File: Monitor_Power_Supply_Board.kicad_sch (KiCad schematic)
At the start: 12 parts, among them J1 Conn_01x02, J2 Conn_01x02, J3 Conn_01x02

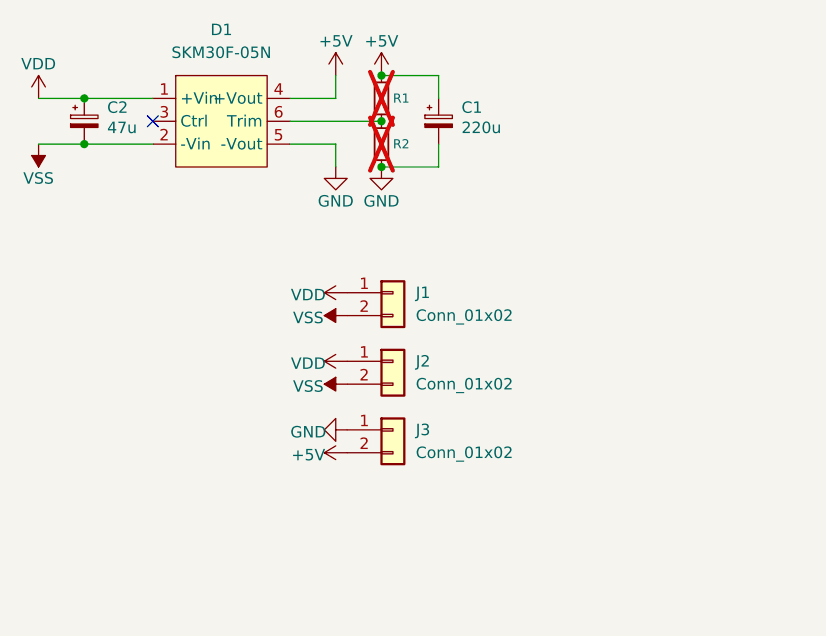
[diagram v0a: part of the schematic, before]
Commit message: VER1.0: добавил разъем для вентилятора и индикацию питания
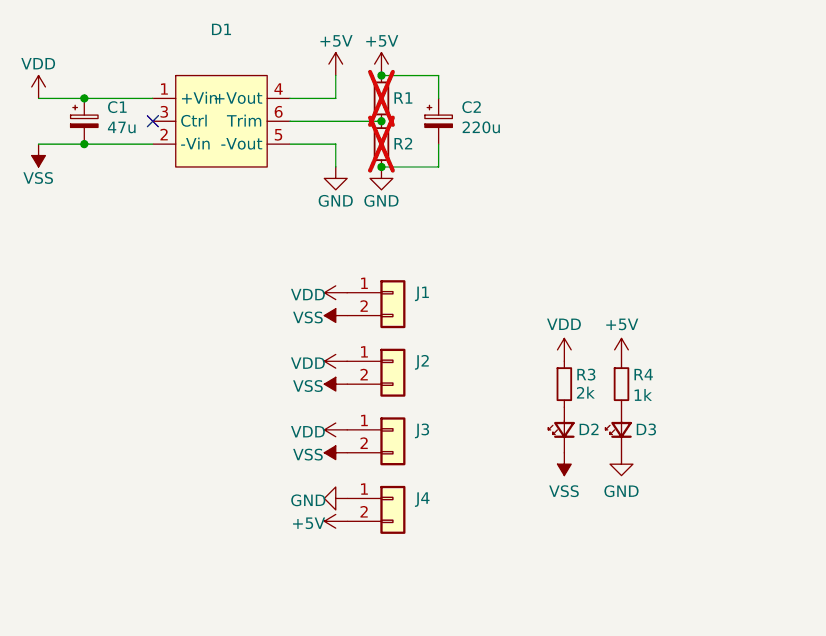
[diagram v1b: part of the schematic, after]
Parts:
- added D2, D3: ~, LED_SMD:LED_0805_2012Metric_Pad1.15x1.40mm_HandSolder, symbol Device:LED_Small
- added J3: ~, Connector_Molex:Molex_Mini-Fit_Jr_5569-02A2_2x01_P4.20mm_Horizontal, symbol Connector_Generic:Conn_01x02
- added R3: 2k, Resistor_SMD:R_0805_2012Metric_Pad1.20x1.40mm_HandSolder, symbol Device:R_Small
- added R4: 1k, Resistor_SMD:R_0805_2012Metric_Pad1.20x1.40mm_HandSolder, symbol Device:R_Small
- C1: renamed from C2; Product Name (none) -> CA45-D025K476T
- C2: renamed from C1; Product Name (none) -> CA45-C010K227T
- D1: value SKM30F-05N -> ~; Product Name (none) -> SKM30F-05N
- J1, J2: value Conn_01x02 -> ~; Product Name (none) -> DS1073-01-2X1MR3T6
- J4: renamed from J3; value Conn_01x02 -> ~; Product Name (none) -> DS1073-01-2X1MR3T6
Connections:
- net +5V: now also R4.1
- net GND: now also D3.1 (K)
- net VDD: now also J3.1 (Pin_1), R3.1
- net VSS: now also D2.1 (K), J3.2 (Pin_2)
- new net: D3.2 (A), R4.2
- new net: D2.2 (A), R3.2
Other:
- moved on the sheet: J4

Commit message: VER1.0: отправил в резонит
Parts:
- C1, C2: Description P/N (none) -> Tantalum Capacitor
- D1: Description P/N (none) -> DCDC
- D2, D3: Description P/N (none) -> Green LED
- J1, J2, J3, J4: Description P/N (none) -> Connector
- R1, R2, R3, R4: Description P/N (none) -> Resistor SMD
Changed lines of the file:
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@@
 			)
 		)
-		(property "Description P/N" ""
+		(property "Description P/N" "Green LED"
 			(at 189.23 130.81 90)
 			(effects
@@
 			)
 		)
-		(property "Description P/N" ""
+		(property "Description P/N" "Connector"
 			(at 163.83 138.43 0)
 			(effects
@@
 			)
 		)
-		(property "Description P/N" ""
+		(property "Description P/N" "Tantalum Capacitor"
 			(at 168.91 96.52 0)
 			(effects
@@
 			)
 		)
-		(property "Description P/N" ""
+		(property "Description P/N" "Connector"
 			(at 163.83 115.57 0)
 			(effects
@@
 			)
 		)
-		(property "Description P/N" ""
+		(property "Description P/N" "Resistor SMD"
 			(at 189.23 125.73 0)
 			(effects
@@
 			)
 		)
-		(property "Description P/N" ""
+		(property "Description P/N" "Tantalum Capacitor"
 			(at 129.54 96.52 0)
 			(effects
@@
 			)
 		)
-		(property "Description P/N" ""
+		(property "Description P/N" "Green LED"
 			(at 182.88 130.81 90)
 			(effects
@@
 			)
 		)
-		(property "Description P/N" ""
+		(property "Description P/N" "Resistor SMD"
 			(at 162.56 99.06 0)
 			(effects
@@
 			)
 		)
-		(property "Description P/N" ""
+		(property "Description P/N" "Resistor SMD"
 			(at 182.88 125.73 0)
 			(effects
@@
 			)
 		)
-		(property "Description P/N" ""
+		(property "Description P/N" "Resistor SMD"
 			(at 162.56 93.98 0)
 			(effects
@@
 			)
 		)
-		(property "Description P/N" ""
+		(property "Description P/N" "Connector"
 			(at 163.83 123.19 0)
 			(effects
@@
 			)
 		)
-		(property "Description P/N" ""
+		(property "Description P/N" "DCDC"
 			(at 144.78 91.44 0)
 			(effects
@@
 			)
 		)
-		(property "Description P/N" ""
+		(property "Description P/N" "Connector"
 			(at 163.83 130.81 0)
 			(effects

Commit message: VER1.0: добавил кд в папку Docs
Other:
- note added: "1 Перечень элементов см. НВЦТ.0001.0600.200 ПЭ3."
- note added: "Индикация питания"
- note added: "Механические отверстия"
- note added: "НВЦТ.0001.0600.200"
- note added: "ООО "Электротранспорнтые"
- note added: "Питание +5В."
- note added: "Разъёмы питания"
- note added: "Схема электрическая соединений"
- note added: "технологии""
- title: (none) -> Плата дисплея
- moved on the sheet: C1, C2, D1, D2, D3, H1, H2, H3, H4, J1, J2, J3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

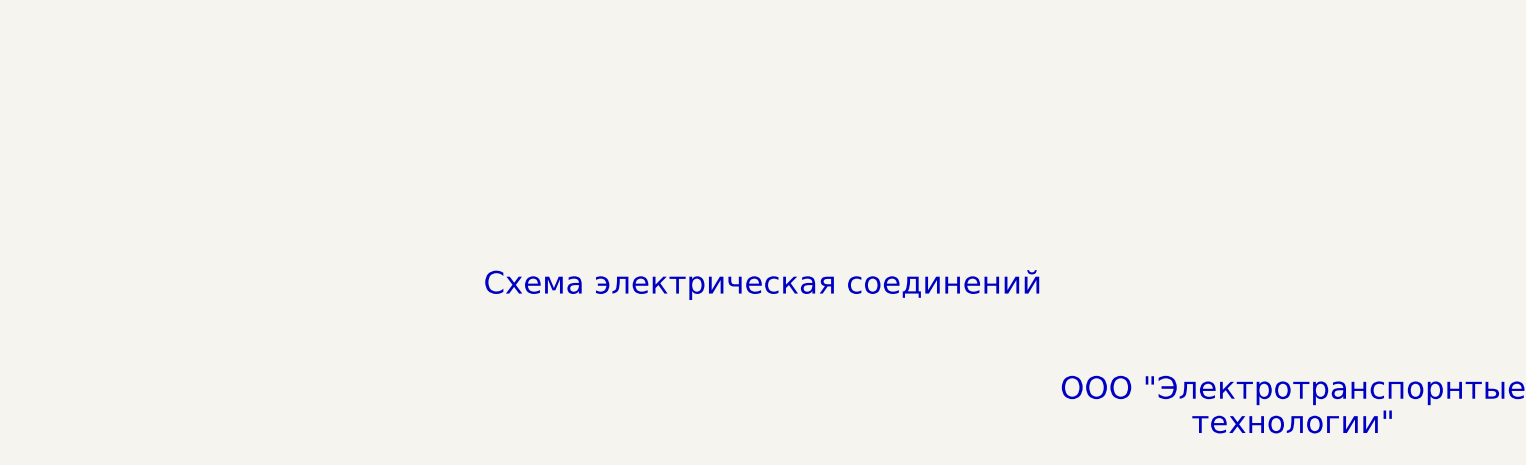
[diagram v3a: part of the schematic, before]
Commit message: VER1.0: исправил Э3
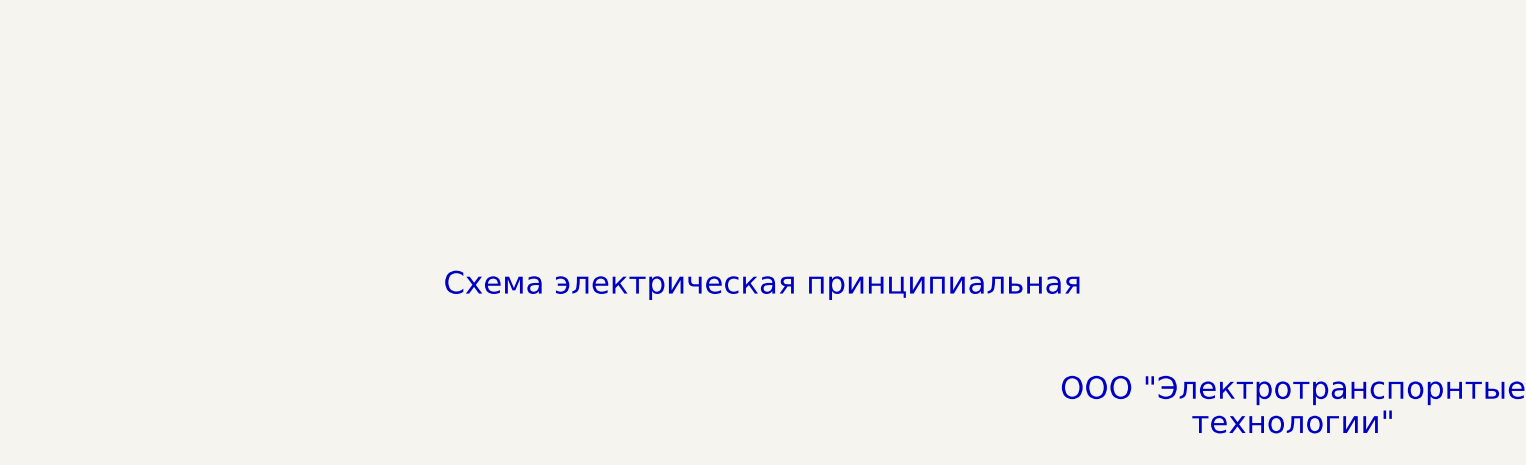
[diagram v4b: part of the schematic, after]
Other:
- note added: "Схема электрическая принципиальная"
- note removed: "Схема электрическая соединений"
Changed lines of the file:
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@@
 		)
 	)
-	(text "Схема электрическая соединений"
+	(text "Схема электрическая принципиальная"
 		(exclude_from_sim no)
 		(at 121.158 271.018 0)
